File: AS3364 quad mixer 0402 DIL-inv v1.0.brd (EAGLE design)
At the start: 41.3 x 16.2 mm, 41 parts, among them IC1 TL072JD, IC2 TL072JD

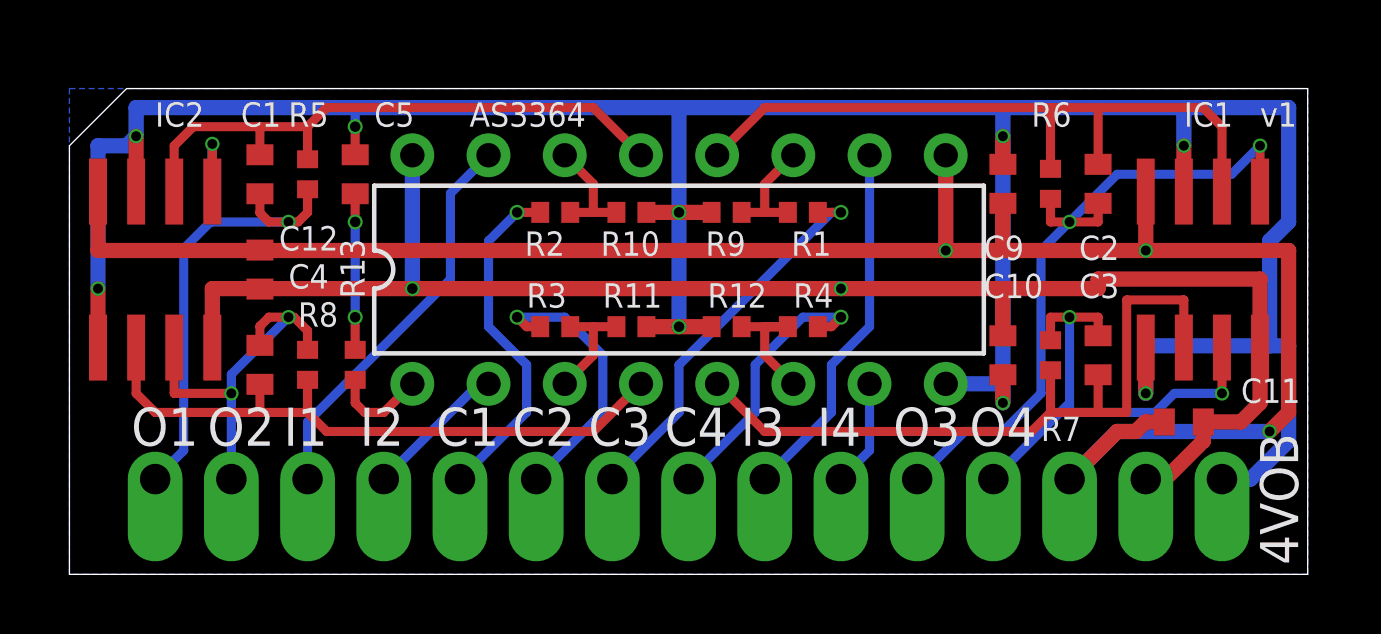
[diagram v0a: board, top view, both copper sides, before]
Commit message: Checked most things, changed CV input resistors, added cap to mixer output
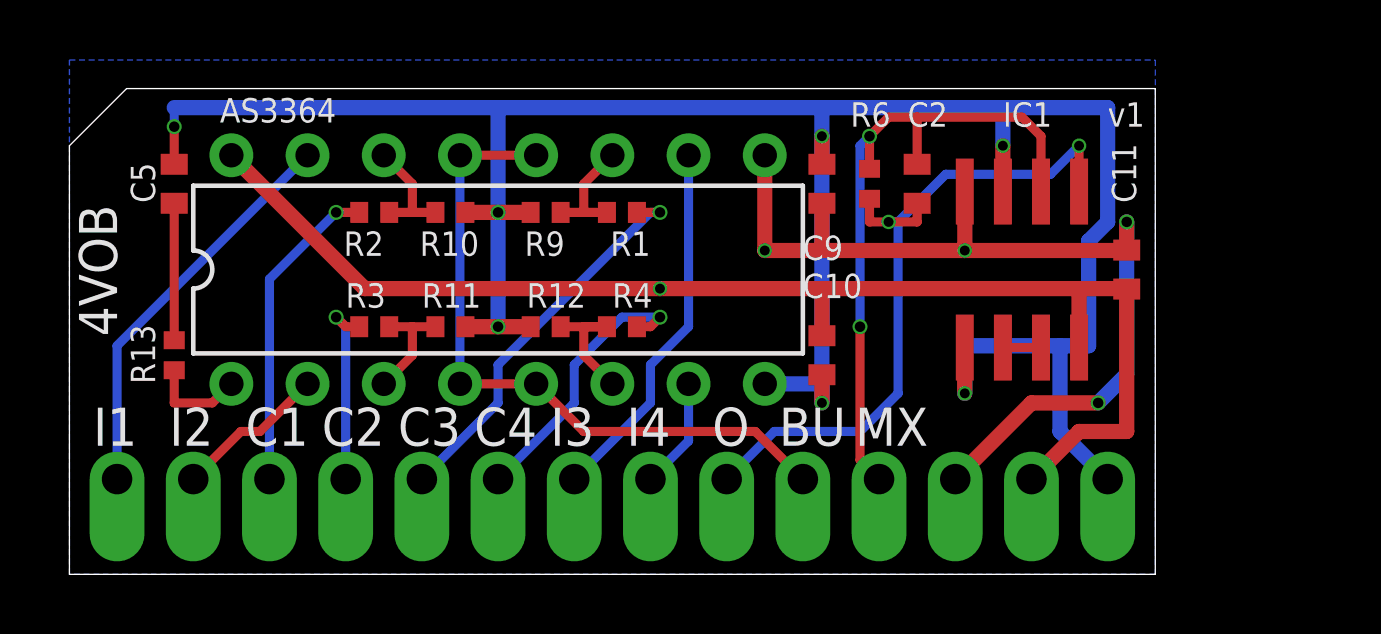
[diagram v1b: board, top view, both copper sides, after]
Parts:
- removed C1, C3, C4: 33pF, rcl:C0402
- removed C12: 100nF, rcl:C0402
- removed IC2: TL072JD, joakim:SO08J
- removed OUT1, OUT2, OUT3, OUT4: (no value), joakim:SIP-PIN01-1J
- removed R5, R7, R8: 47k, rcl:R0402
- added BUS, MIX, OUT: (no value), joakim:SIP-PIN01-1J
- moved IN4 6.35 mm to (19.4, 3.17)
- moved CV1 6.35 mm to (6.67, 3.17)
- moved CV2 6.35 mm to (9.21, 3.17)
- moved CV3 6.35 mm to (11.7, 3.17)
- moved CV4 6.35 mm to (14.3, 3.17)
- moved IN1 6.35 mm to (1.59, 3.17)
- moved IN2 6.35 mm to (4.13, 3.17)
- moved IN3 6.35 mm to (16.8, 3.17)
- moved C5 6.04 mm to (3.49, 13.0)
- moved R13 6.04 mm to (3.49, 7.30)
- moved R1 6.03 mm to (18.4, 12.1)
- moved R10 6.03 mm to (12.7, 12.1)
- moved R11 6.03 mm to (12.7, 8.26)
- moved R4 6.03 mm to (18.4, 8.26)
- moved DA2 6.03 mm to (14.3, 10.2)
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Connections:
- removed net N$1: C4.1, DA2.4, IC2.6, R8.1
- removed net N$3: C3.1, DA2.5, IC1.6, R7.1
- removed net N$5: C2.1, DA2.12, IC1.2, R6.1
- removed net N$7: C1.1, DA2.13, IC2.2, R5.1
- removed net OUT1: C1.2, IC2.1, OUT1.1, R5.2
- removed net OUT2: C4.2, IC2.7, OUT2.1, R8.2
- removed net OUT3: C2.2, IC1.1, OUT3.1, R6.2
- removed net OUT4: C3.2, IC1.7, OUT4.1, R7.2
- new net BUS: BUS.1, DA2.12, DA2.13, DA2.4, DA2.5
- new net MIX: C2.1, IC1.2, MIX.1, R6.1
- new net NC1: IC1.6, IC1.7
- new net OUT: C2.2, IC1.1, OUT.1, R6.2
- net +12V: no longer C12.2, IC2.8
- net -12V: no longer C12.1, IC2.4
- net GND: no longer IC2.3, IC2.5
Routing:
- net -12V: track 65.9 -> 32.0 mm, vias 3 -> 4
- net OUT: track 0.00 -> 24.5 mm, vias 0 -> 2
- net N$3: track 24.5 -> 0.00 mm
- net N$5: track 23.8 -> 0.00 mm
- net OUT3: track 23.3 -> 0.00 mm, vias 2 -> 0
- net BUS: track 0.00 -> 22.9 mm
- net MIX: track 0.00 -> 22.6 mm, vias 0 -> 2
- net OUT1: track 21.9 -> 0.00 mm, vias 2 -> 0
- net N$1: track 21.6 -> 0.00 mm
- net N$7: track 20.3 -> 0.00 mm
- net GND: track 101.0 -> 81.6 mm, vias 9 -> 7
- net OUT4: track 16.6 -> 0.00 mm, vias 2 -> 0
- net OUT2: track 12.8 -> 0.00 mm, vias 2 -> 0
- net +12V: track 52.6 -> 43.8 mm, vias 2 -> 1
- net CV2: track 9.33 -> 6.43 mm
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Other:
- board size 41.3 x 16.2 mm -> 36.2 x 16.2 mm
- board text added: "BU"
- board text added: "MX"
- board text added: "O"
- board text added: "Quad lin mixer"
- board text removed: "O1"
- board text removed: "O2"
- board text removed: "O3"
- board text removed: "O4"
- board text removed: "Quad lin inv VCA"

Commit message: Almost finished bom/cpl
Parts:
- removed +12V, -12V, BUS, CV1, CV2, CV3, CV4, GND, IN1, IN2, IN3, IN4, MIX, OUT: (no value), joakim:SIP-PIN01-1J
- added U$2, U$3: MA07-1JP, joakim:SIP-PIN07-1J
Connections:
- net +12V: now also U$2.6; no longer +12V.1
- net -12V: now also U$2.5; no longer -12V.1
- net BUS: now also U$2.3; no longer BUS.1
- net CV1: now also U$3.3; no longer CV1.1
- net CV2: now also U$3.4; no longer CV2.1
- net CV3: now also U$3.5; no longer CV3.1
- net CV4: now also U$3.6; no longer CV4.1
- net GND: now also U$2.7; no longer GND.1
- net IN1: now also U$3.1; no longer IN1.1
- net IN2: now also U$3.2; no longer IN2.1
- net IN3: now also U$3.7; no longer IN3.1
- net IN4: now also U$2.1; no longer IN4.1
- net MIX: now also U$2.4; no longer MIX.1
- net OUT: now also U$2.2; no longer OUT.1
